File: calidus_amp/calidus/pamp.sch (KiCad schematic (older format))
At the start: 50 parts, among them U4 TDA7293, U5 TDA7293

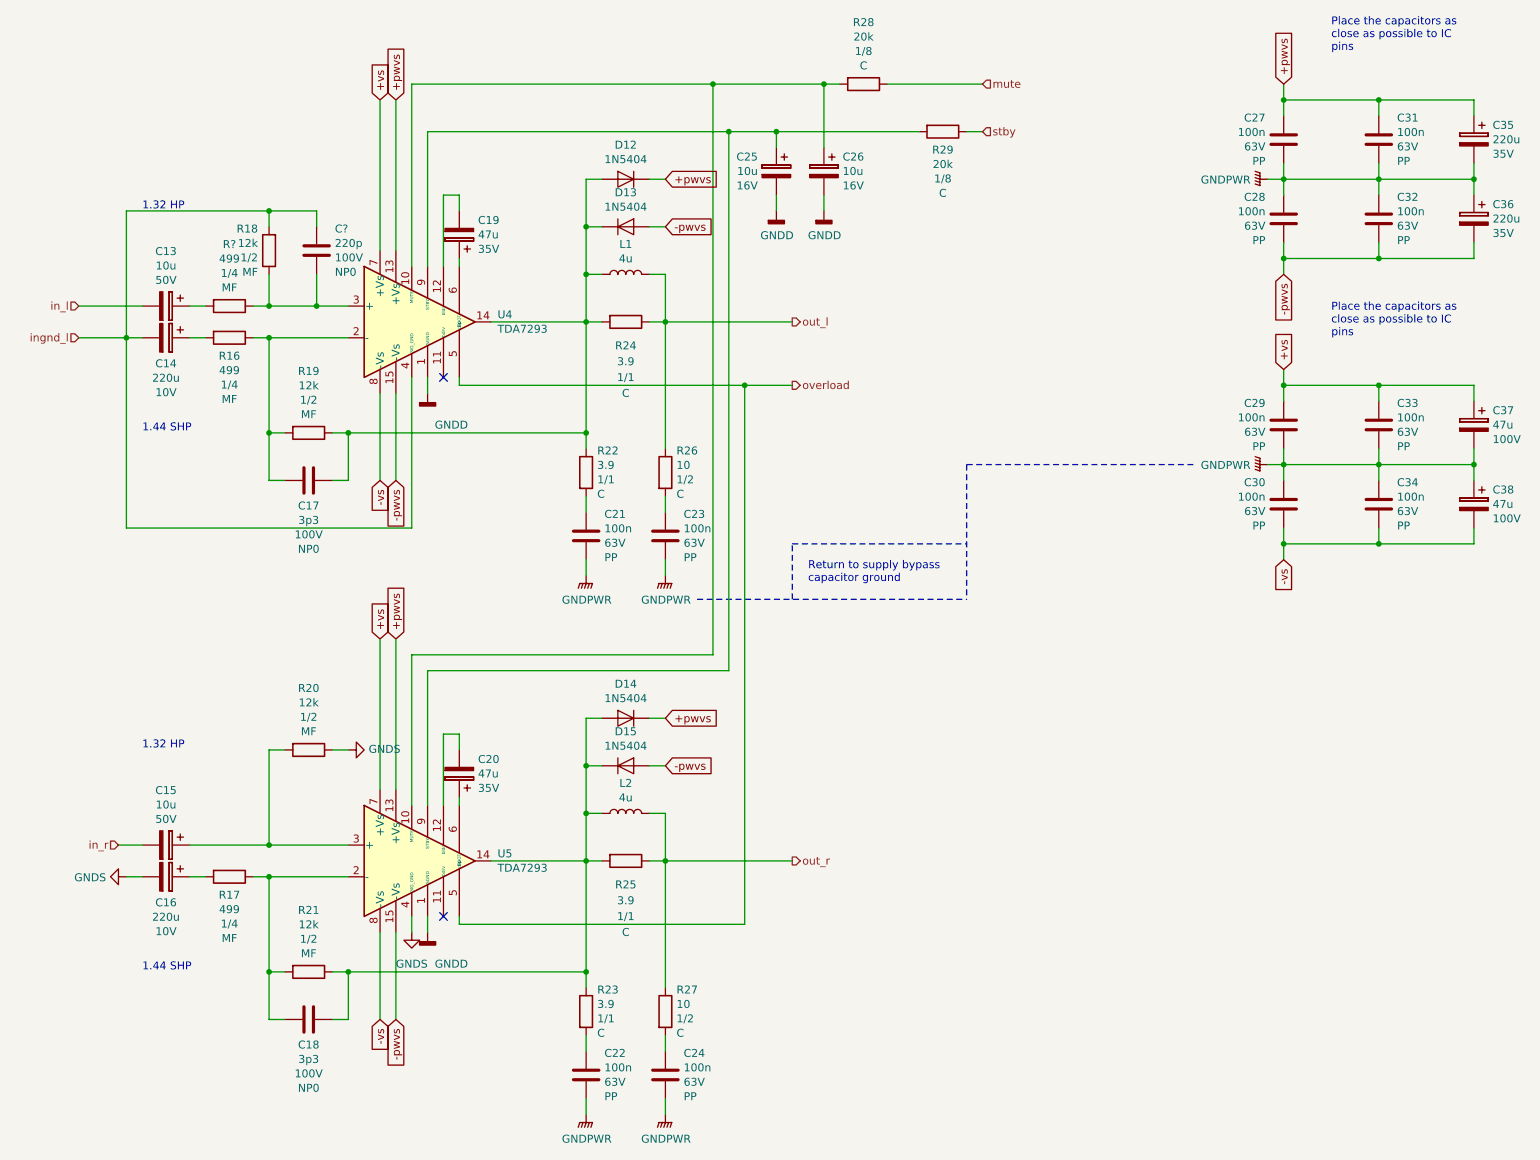
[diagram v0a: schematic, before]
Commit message: WIP: Component placement on PCB
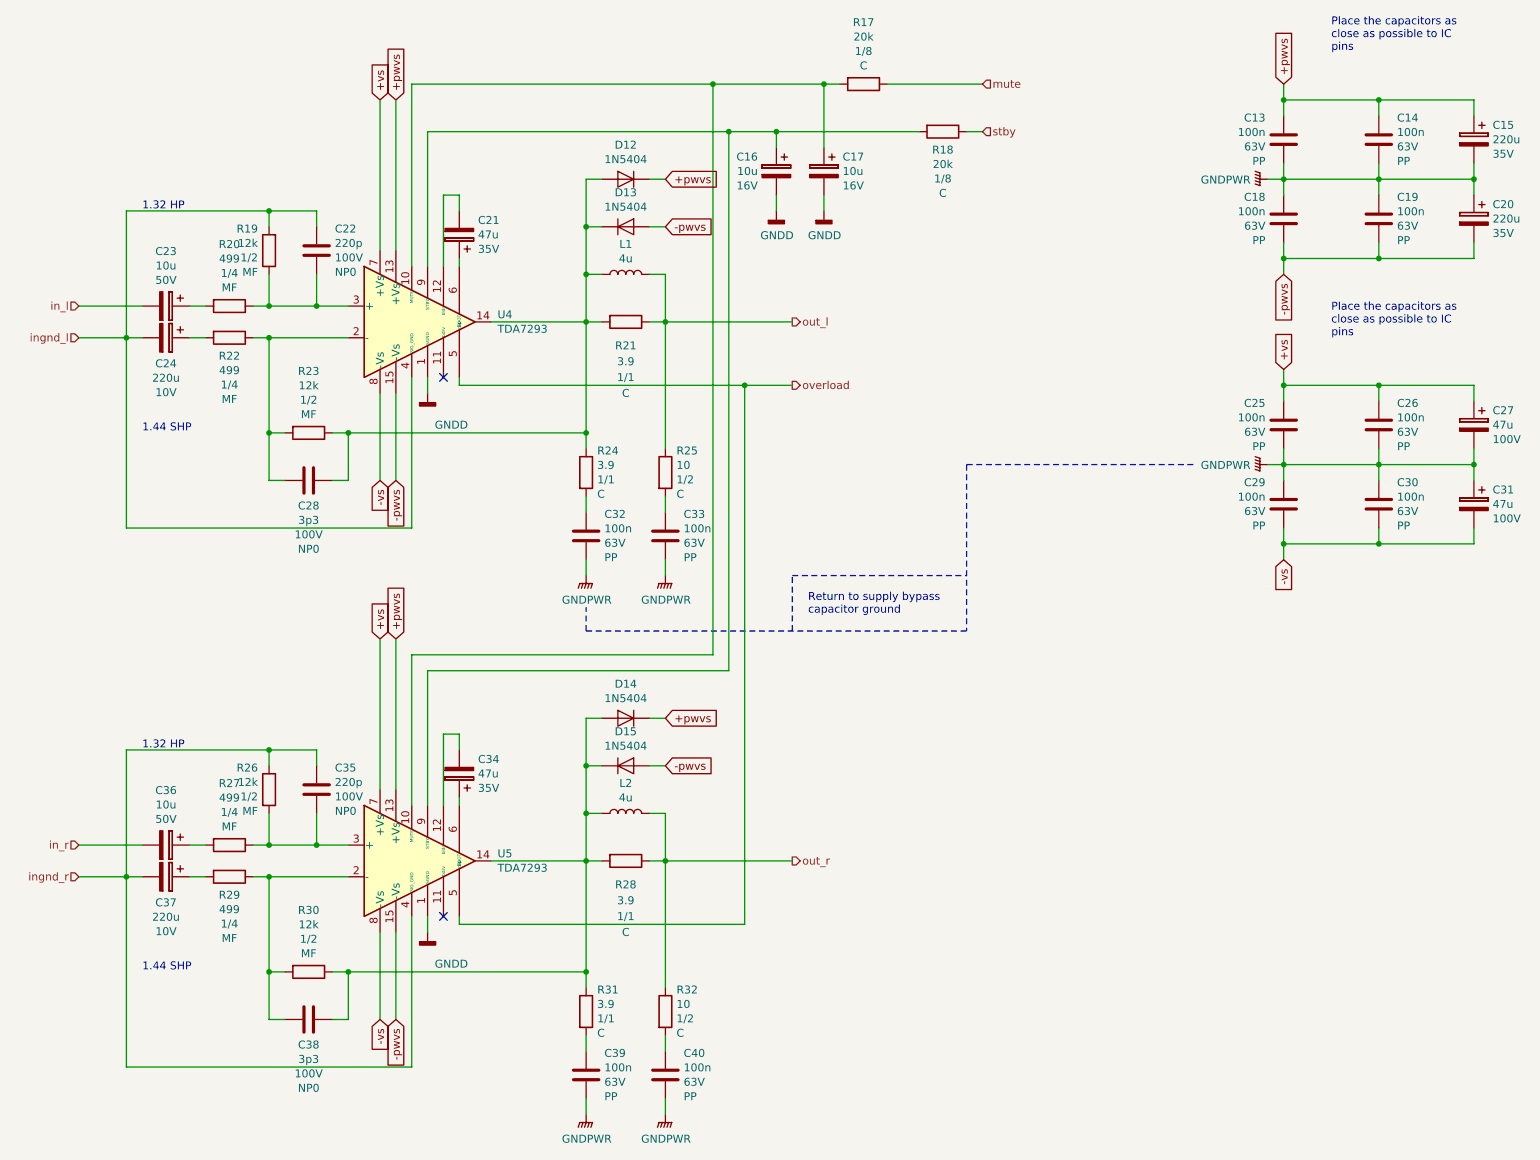
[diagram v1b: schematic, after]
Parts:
- added C35: 220p, Capacitor_THT:C_Disc_D3.0mm_W1.6mm_P2.50mm, symbol Device:C
- added R27: 499, Resistor_THT:R_Axial_DIN0207_L6.3mm_D2.5mm_P7.62mm_Horizontal, symbol Device:R
- gave numbers to parts that had none: 2
- renumbered C27 to C13, C31 to C14, C35 to C15, C25 to C16, C26 to C17, C28 to C18, C32 to C19, C36 to C20, C19 to C21, C13 to C23, C14 to C24, C29 to C25, C33 to C26, C37 to C27, C17 to C28, C30 to C29, C34 to C30, C38 to C31, C21 to C32, C23 to C33, C20 to C34, C15 to C36, C16 to C37, C18 to C38, C22 to C39, C24 to C40, R28 to R17, R29 to R18, R18 to R19, R24 to R21, R16 to R22, R19 to R23, R22 to R24, R26 to R25, R20 to R26, R25 to R28, R17 to R29, R21 to R30, R23 to R31, R27 to R32
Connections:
- net at R26.2, U5.3 (+): now also C35.1, R27.1; no longer C36.1
- net GNDS renamed ingnd_r
- net ingnd_r: now also C35.2
- new net: C36.1, R27.2
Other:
- moved on the sheet: R26

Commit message: WIP: Component placement
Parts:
- added C16, C22: 220u, Capacitor_THT:CP_Radial_D10.0mm_P5.00mm, symbol Device:CP
- added C30, C35: 47u, Capacitor_THT:CP_Radial_D10.0mm_P5.00mm, symbol Device:CP
- renumbered C16 to C17, C17 to C18, C18 to C19, C19 to C20, C20 to C21, C21 to C23, C22 to C24, C23 to C25, C24 to C26, C25 to C27, C26 to C28, C27 to C29, C28 to C31, C29 to C32, C30 to C33, C31 to C34, C32 to C36, C33 to C37, C34 to C38, C35 to C39, C36 to C40, C37 to C41, C38 to C42, C39 to C43, C40 to C44
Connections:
- net +pwvs: now also C16.1
- net +vs: now also C30.1
- net -pwvs: now also C22.2
- net -vs: now also C35.2
- net GNDPWR: now also C16.2, C22.1, C30.2, C35.1
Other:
- moved on the sheet: C13, C14, C15, C19, C20, C21, C27, C28, C29, C32, C33, C34

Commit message: WIP: Component placement and footpring assignment
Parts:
- C23, C38: Manufacturer Rybicon:35YXF47MEFC6.3X11 -> Rybicon:50YXF47MEFC6.3X11; Supplier1 Farnell:1144626 -> Farnell:1144633; Voltage 35V -> 50V
- C29, C30, C34, C35: footprint Capacitor_THT:CP_Radial_D10.0mm_P5.00mm -> Capacitor_THT:CP_Radial_D6.3mm_P2.50mm; Manufacturer Rybicon:100YXF47MEFC10X16 -> Rybicon:50YXF47MEFC6.3X11; Supplier1 Farnell:1144641 -> Farnell:1144633; Voltage 100V -> 50V
- D12, D13, D14, D15: footprint Diode_THT:D_DO-35_SOD27_P10.16mm_Horizontal -> Diode_THT:D_DO-35_SOD27_P7.62mm_Horizontal
- R20, R22, R27, R29: footprint Resistor_THT:R_Axial_DIN0207_L6.3mm_D2.5mm_P7.62mm_Horizontal -> Resistor_THT:R_Axial_DIN0207_L6.3mm_D2.5mm_P10.16mm_Horizontal
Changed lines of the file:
@@
 Text Notes 2100 1800 0    50   ~ 0
 1.32 HP
-$Comp
-L Device:CP C23
-U 1 1 5C37FBD5
-P 4100 1950
-F 0 "C23" H 3982 1859 50  0000 R CNN
-F 1 "47u" H 3982 1950 50  0000 R CNN
-F 2 "Capacitor_THT:CP_Radial_D6.3mm_P2.50mm" H 4138 1800 50  0001 C CNN
-F 3 "http://www.farnell.com/datasheets/2321304.pdf" H 4100 1950 50  0001 C CNN
-F 4 "35V" H 3982 2041 50  0000 R CNN "Voltage"
-F 5 "Rybicon:35YXF47MEFC6.3X11" H 4100 1950 50  0001 C CNN "Manufacturer"
-F 6 "Farnell:1144626" H 4100 1950 50  0001 C CNN "Supplier1"
-	1    4100 1950
-	-1   0    0    1
-$EndComp
 Wire Wire Line
 	4100 2150 4100 2100
@@
 F 0 "D13" H 5150 2116 50  0000 C CNN
 F 1 "1N5404" H 5150 2025 50  0000 C CNN
-F 2 "Diode_THT:D_DO-35_SOD27_P10.16mm_Horizontal" H 5150 1900 50  0001 C CNN
+F 2 "Diode_THT:D_DO-35_SOD27_P7.62mm_Horizontal" H 5150 1900 50  0001 C CNN
 F 3 "~" H 5150 1900 50  0001 C CNN
 	1    5150 1900
@@
 F 0 "D12" H 5150 1816 50  0000 C CNN
 F 1 "1N5404" H 5150 1725 50  0000 C CNN
-F 2 "Diode_THT:D_DO-35_SOD27_P10.16mm_Horizontal" H 5150 1600 50  0001 C CNN
+F 2 "Diode_THT:D_DO-35_SOD27_P7.62mm_Horizontal" H 5150 1600 50  0001 C CNN
 F 3 "~" H 5150 1600 50  0001 C CNN
 	1    5150 1600
@@
 F 0 "D15" H 5150 5516 50  0000 C CNN
 F 1 "1N5404" H 5150 5425 50  0000 C CNN
-F 2 "Diode_THT:D_DO-35_SOD27_P10.16mm_Horizontal" H 5150 5300 50  0001 C CNN
+F 2 "Diode_THT:D_DO-35_SOD27_P7.62mm_Horizontal" H 5150 5300 50  0001 C CNN
 F 3 "~" H 5150 5300 50  0001 C CNN
 	1    5150 5300
@@
 F 0 "D14" H 5150 5216 50  0000 C CNN
 F 1 "1N5404" H 5150 5125 50  0000 C CNN
-F 2 "Diode_THT:D_DO-35_SOD27_P10.16mm_Horizontal" H 5150 5000 50  0001 C CNN
+F 2 "Diode_THT:D_DO-35_SOD27_P7.62mm_Horizontal" H 5150 5000 50  0001 C CNN
 F 3 "~" H 5150 5000 50  0001 C CNN
 	1    5150 5000
@@
 F 0 "R22" V 2765 2600 50  0000 C CNN
 F 1 "499" V 2856 2600 50  0000 C CNN
-F 2 "Resistor_THT:R_Axial_DIN0207_L6.3mm_D2.5mm_P7.62mm_Horizontal" V 2580 2600 50  0001 C CNN
+F 2 "Resistor_THT:R_Axial_DIN0207_L6.3mm_D2.5mm_P10.16mm_Horizontal" V 2580 2600 50  0001 C CNN
 F 3 "~" H 2650 2600 50  0001 C CNN
 F 4 "1/4" V 2947 2600 50  0000 C CNN "Power"
@@
 F 0 "R29" V 2765 6000 50  0000 C CNN
 F 1 "499" V 2856 6000 50  0000 C CNN
-F 2 "Resistor_THT:R_Axial_DIN0207_L6.3mm_D2.5mm_P7.62mm_Horizontal" V 2580 6000 50  0001 C CNN
+F 2 "Resistor_THT:R_Axial_DIN0207_L6.3mm_D2.5mm_P10.16mm_Horizontal" V 2580 6000 50  0001 C CNN
 F 3 "~" H 2650 6000 50  0001 C CNN
 F 4 "1/4" V 2947 6000 50  0000 C CNN "Power"
@@
 Place the capacitors as\nclose as possible to IC\npins
 $Comp
-L Device:CP C38
-U 1 1 5C5AF4B7
-P 4100 5350
-F 0 "C38" H 3982 5259 50  0000 R CNN
-F 1 "47u" H 3982 5350 50  0000 R CNN
-F 2 "Capacitor_THT:CP_Radial_D6.3mm_P2.50mm" H 4138 5200 50  0001 C CNN
-F 3 "http://www.farnell.com/datasheets/2321304.pdf" H 4100 5350 50  0001 C CNN
-F 4 "35V" H 3982 5441 50  0000 R CNN "Voltage"
-F 5 "Rybicon:35YXF47MEFC6.3X11" H 4100 5350 50  0001 C CNN "Manufacturer"
-F 6 "Farnell:1144626" H 4100 5350 50  0001 C CNN "Supplier1"
-	1    4100 5350
-	-1   0    0    1
-$EndComp
-$Comp
 L Device:CP C?
 U 1 1 5C5B3FFC
@@
 F 0 "C29" H 9782 3241 50  0000 R CNN
 F 1 "47u" H 9782 3150 50  0000 R CNN
-F 2 "Capacitor_THT:CP_Radial_D10.0mm_P5.00mm" H 9938 3000 50  0001 C CNN
-F 3 "http://www.farnell.com/datasheets/2124421.pdf" H 9900 3150 50  0001 C CNN
-F 4 "100V" H 9782 3059 50  0000 R CNN "Voltage"
-F 5 "Rybicon:100YXF47MEFC10X16" H 9900 3150 50  0001 C CNN "Manufacturer"
-F 6 "Farnell:1144641" H 9900 3150 50  0001 C CNN "Supplier1"
+F 2 "Capacitor_THT:CP_Radial_D6.3mm_P2.50mm" H 9938 3000 50  0001 C CNN
+F 3 "http://www.farnell.com/datasheets/2321304.pdf" H 9900 3150 50  0001 C CNN
+F 4 "50V" H 9782 3059 50  0000 R CNN "Voltage"
+F 5 "Rybicon:50YXF47MEFC6.3X11" H 9900 3150 50  0001 C CNN "Manufacturer"
+F 6 "Farnell:1144633" H 9900 3150 50  0001 C CNN "Supplier1"
 	1    9900 3150
-	-1   0    0    -1
-$EndComp
-$Comp
-L Device:CP C?
-U 1 1 5C5CD581
-P 9900 3650
-AR Path="/5C37BC48/5C5CD581" Ref="C?"  Part="1"
-AR Path="/5C37BC7C/5C5CD581" Ref="C34"  Part="1"
-F 0 "C34" H 9782 3741 50  0000 R CNN
-F 1 "47u" H 9782 3650 50  0000 R CNN
-F 2 "Capacitor_THT:CP_Radial_D10.0mm_P5.00mm" H 9938 3500 50  0001 C CNN
-F 3 "http://www.farnell.com/datasheets/2124421.pdf" H 9900 3650 50  0001 C CNN
-F 4 "100V" H 9782 3559 50  0000 R CNN "Voltage"
-F 5 "Rybicon:100YXF47MEFC10X16" H 9900 3650 50  0001 C CNN "Manufacturer"
-F 6 "Farnell:1144641" H 9900 3650 50  0001 C CNN "Supplier1"
-	1    9900 3650
 	-1   0    0    -1
 $EndComp
@@
 F 0 "R20" V 2261 2400 50  0000 C CNN
 F 1 "499" V 2352 2400 50  0000 C CNN
-F 2 "Resistor_THT:R_Axial_DIN0207_L6.3mm_D2.5mm_P7.62mm_Horizontal" V 2580 2400 50  0001 C CNN
+F 2 "Resistor_THT:R_Axial_DIN0207_L6.3mm_D2.5mm_P10.16mm_Horizontal" V 2580 2400 50  0001 C CNN
 F 3 "~" H 2650 2400 50  0001 C CNN
 F 4 "1/4" V 2443 2400 50  0000 C CNN "Power"
@@
 F 0 "R27" V 2261 5800 50  0000 C CNN
 F 1 "499" V 2352 5800 50  0000 C CNN
-F 2 "Resistor_THT:R_Axial_DIN0207_L6.3mm_D2.5mm_P7.62mm_Horizontal" V 2580 5800 50  0001 C CNN
+F 2 "Resistor_THT:R_Axial_DIN0207_L6.3mm_D2.5mm_P10.16mm_Horizontal" V 2580 5800 50  0001 C CNN
 F 3 "~" H 2650 5800 50  0001 C CNN
 F 4 "1/4" V 2443 5800 50  0000 C CNN "Power"
@@
 Wire Wire Line
 	10500 3800 10500 3900
-$Comp
-L Device:CP C?
-U 1 1 5C542595
-P 10500 3150
-AR Path="/5C37BC48/5C542595" Ref="C?"  Part="1"
-AR Path="/5C37BC7C/5C542595" Ref="C30"  Part="1"
-F 0 "C30" H 10382 3241 50  0000 R CNN
-F 1 "47u" H 10382 3150 50  0000 R CNN
-F 2 "Capacitor_THT:CP_Radial_D10.0mm_P5.00mm" H 10538 3000 50  0001 C CNN
-F 3 "http://www.farnell.com/datasheets/2124421.pdf" H 10500 3150 50  0001 C CNN
-F 4 "100V" H 10382 3059 50  0000 R CNN "Voltage"
-F 5 "Rybicon:100YXF47MEFC10X16" H 10500 3150 50  0001 C CNN "Manufacturer"
-F 6 "Farnell:1144641" H 10500 3150 50  0001 C CNN "Supplier1"
-	1    10500 3150
-	-1   0    0    -1
-$EndComp
-$Comp
-L Device:CP C?
-U 1 1 5C54259F
-P 10500 3650
-AR Path="/5C37BC48/5C54259F" Ref="C?"  Part="1"
-AR Path="/5C37BC7C/5C54259F" Ref="C35"  Part="1"
-F 0 "C35" H 10382 3741 50  0000 R CNN
-F 1 "47u" H 10382 3650 50  0000 R CNN
-F 2 "Capacitor_THT:CP_Radial_D10.0mm_P5.00mm" H 10538 3500 50  0001 C CNN
-F 3 "http://www.farnell.com/datasheets/2124421.pdf" H 10500 3650 50  0001 C CNN
-F 4 "100V" H 10382 3559 50  0000 R CNN "Voltage"
-F 5 "Rybicon:100YXF47MEFC10X16" H 10500 3650 50  0001 C CNN "Manufacturer"
-F 6 "Farnell:1144641" H 10500 3650 50  0001 C CNN "Supplier1"
-	1    10500 3650
-	-1   0    0    -1
-$EndComp
 Connection ~ 9900 2900
 Connection ~ 9900 3900
 Connection ~ 9900 2100
 Connection ~ 9900 1100
+$Comp
+L Device:CP C?
+U 1 1 5C52C9EF
+P 9900 3650
+AR Path="/5C37BC48/5C52C9EF" Ref="C?"  Part="1"
+AR Path="/5C37BC7C/5C52C9EF" Ref="C34"  Part="1"
+F 0 "C34" H 9782 3741 50  0000 R CNN
+F 1 "47u" H 9782 3650 50  0000 R CNN
+F 2 "Capacitor_THT:CP_Radial_D6.3mm_P2.50mm" H 9938 3500 50  0001 C CNN
+F 3 "http://www.farnell.com/datasheets/2321304.pdf" H 9900 3650 50  0001 C CNN
+F 4 "50V" H 9782 3559 50  0000 R CNN "Voltage"
+F 5 "Rybicon:50YXF47MEFC6.3X11" H 9900 3650 50  0001 C CNN "Manufacturer"
+F 6 "Farnell:1144633" H 9900 3650 50  0001 C CNN "Supplier1"
+	1    9900 3650
+	-1   0    0    -1
+$EndComp
+$Comp
+L Device:CP C?
+U 1 1 5C52D5BD
+P 10500 3150
+AR Path="/5C37BC48/5C52D5BD" Ref="C?"  Part="1"
+AR Path="/5C37BC7C/5C52D5BD" Ref="C30"  Part="1"
+F 0 "C30" H 10382 3241 50  0000 R CNN
+F 1 "47u" H 10382 3150 50  0000 R CNN
+F 2 "Capacitor_THT:CP_Radial_D6.3mm_P2.50mm" H 10538 3000 50  0001 C CNN
+F 3 "http://www.farnell.com/datasheets/2321304.pdf" H 10500 3150 50  0001 C CNN
+F 4 "50V" H 10382 3059 50  0000 R CNN "Voltage"
+F 5 "Rybicon:50YXF47MEFC6.3X11" H 10500 3150 50  0001 C CNN "Manufacturer"
+F 6 "Farnell:1144633" H 10500 3150 50  0001 C CNN "Supplier1"
+	1    10500 3150
+	-1   0    0    -1
+$EndComp
+$Comp
+L Device:CP C?
+U 1 1 5C52D6FF
+P 10500 3650
+AR Path="/5C37BC48/5C52D6FF" Ref="C?"  Part="1"
+AR Path="/5C37BC7C/5C52D6FF" Ref="C35"  Part="1"
+F 0 "C35" H 10382 3741 50  0000 R CNN
+F 1 "47u" H 10382 3650 50  0000 R CNN
+F 2 "Capacitor_THT:CP_Radial_D6.3mm_P2.50mm" H 10538 3500 50  0001 C CNN
+F 3 "http://www.farnell.com/datasheets/2321304.pdf" H 10500 3650 50  0001 C CNN
+F 4 "50V" H 10382 3559 50  0000 R CNN "Voltage"
+F 5 "Rybicon:50YXF47MEFC6.3X11" H 10500 3650 50  0001 C CNN "Manufacturer"
+F 6 "Farnell:1144633" H 10500 3650 50  0001 C CNN "Supplier1"
+	1    10500 3650
+	-1   0    0    -1
+$EndComp
+$Comp
+L Device:CP C?
+U 1 1 5C5349E4
+P 4100 1950
+AR Path="/5C37BC48/5C5349E4" Ref="C?"  Part="1"
+AR Path="/5C37BC7C/5C5349E4" Ref="C23"  Part="1"
+F 0 "C23" H 3982 1859 50  0000 R CNN
+F 1 "47u" H 3982 1950 50  0000 R CNN
+F 2 "Capacitor_THT:CP_Radial_D6.3mm_P2.50mm" H 4138 1800 50  0001 C CNN
+F 3 "http://www.farnell.com/datasheets/2321304.pdf" H 4100 1950 50  0001 C CNN
+F 4 "50V" H 3982 2041 50  0000 R CNN "Voltage"
+F 5 "Rybicon:50YXF47MEFC6.3X11" H 4100 1950 50  0001 C CNN "Manufacturer"
+F 6 "Farnell:1144633" H 4100 1950 50  0001 C CNN "Supplier1"
+	1    4100 1950
+	-1   0    0    1
+$EndComp
+$Comp
+L Device:CP C?
+U 1 1 5C535B08
+P 4100 5350
+AR Path="/5C37BC48/5C535B08" Ref="C?"  Part="1"
+AR Path="/5C37BC7C/5C535B08" Ref="C38"  Part="1"
+F 0 "C38" H 3982 5259 50  0000 R CNN
+F 1 "47u" H 3982 5350 50  0000 R CNN
+F 2 "Capacitor_THT:CP_Radial_D6.3mm_P2.50mm" H 4138 5200 50  0001 C CNN
+F 3 "http://www.farnell.com/datasheets/2321304.pdf" H 4100 5350 50  0001 C CNN
+F 4 "50V" H 3982 5441 50  0000 R CNN "Voltage"
+F 5 "Rybicon:50YXF47MEFC6.3X11" H 4100 5350 50  0001 C CNN "Manufacturer"
+F 6 "Farnell:1144633" H 4100 5350 50  0001 C CNN "Supplier1"
+	1    4100 5350
+	-1   0    0    1
+$EndComp
 $EndSCHEMATC
